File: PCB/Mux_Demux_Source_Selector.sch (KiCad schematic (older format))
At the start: 2 parts, among them U3 4052

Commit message: Libraries and footprints adjustments. New connectors (4 pins main, 2 pins debug and 6 pins isp). New source input cap.
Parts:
- R1: symbol R-RESCUE-ArduBooster -> R
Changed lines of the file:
@@
 EESchema Schematic File Version 2
-LIBS:ArduBooster-rescue
 LIBS:power
 LIBS:device
@@
 Rev "1.0"
 Comp ""
-Comment1 "If OUTPUT_SELECTION is \"0\", pedal signal is used."
-Comment2 "If OUTPUT_SELECTION is \"1\", Arduino signal is used."
-Comment3 ""
-Comment4 ""
+Comment1 "If OUTPUT_SELECTION is \"0\", pedal signal is used"
+Comment2 "If OUTPUT_SELECTION is \"1\", Arduino signal is used"
+Comment3 "Used as workaround to Arduino boot dalay"
+Comment4 "Select output source"
 $EndDescr
 $Comp
@@
 Connection ~ 4950 4400
 $Comp
-L R-RESCUE-ArduBooster R1
+L R R1
 U 1 1 54D7D7B4
 P 4700 4350
@@
 	4850 4050 4200 4050
 Wire Wire Line
-	4700 4050 4700 4100
+	4700 4050 4700 4200
 Wire Wire Line
-	4700 4650 4700 4600
+	4700 4650 4700 4500
 Connection ~ 4950 4650
 Connection ~ 4700 4050

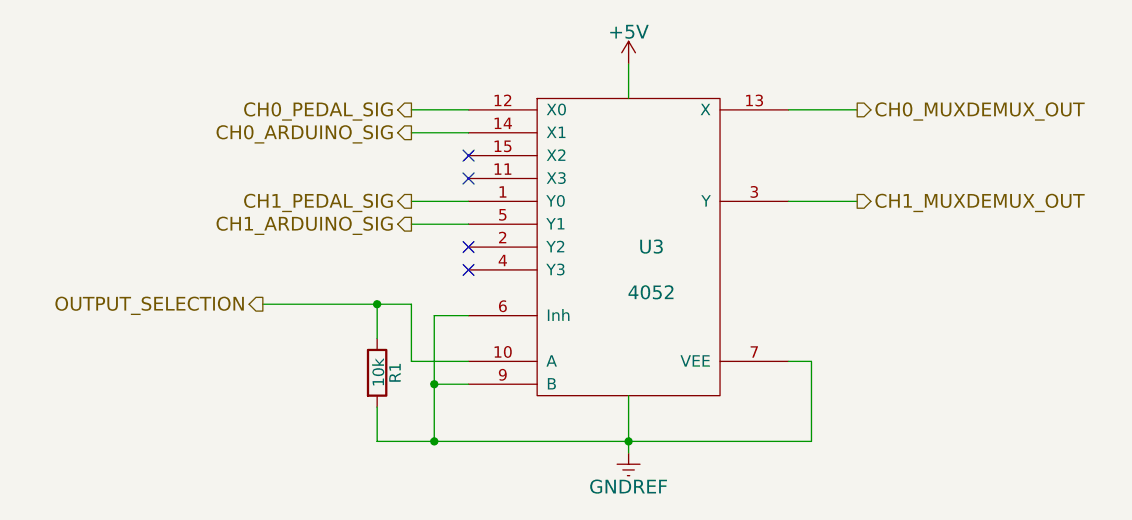
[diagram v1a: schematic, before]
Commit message: New connectors connection. Labels corrections (direction).
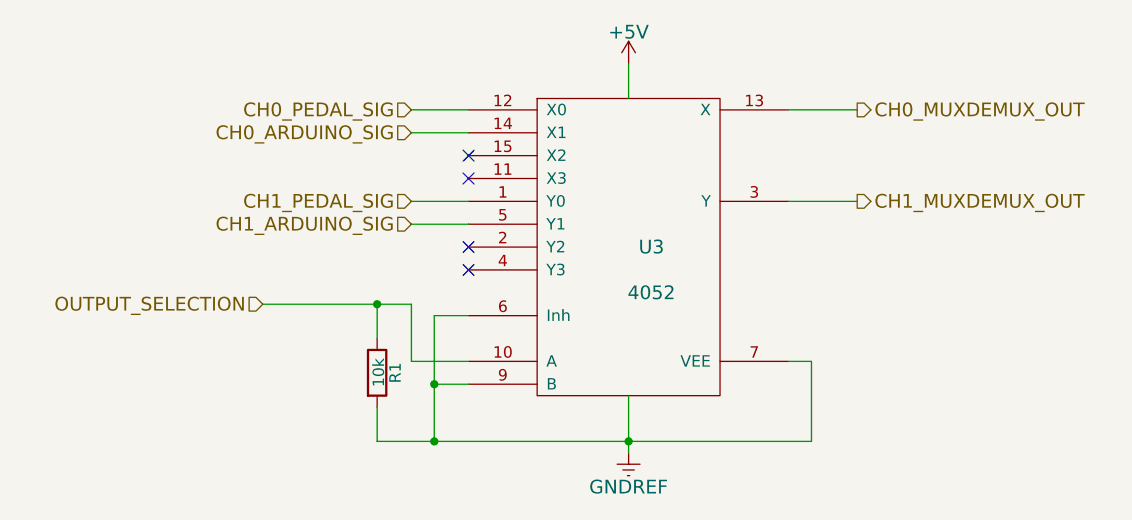
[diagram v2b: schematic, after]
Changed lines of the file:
@@
 $EndComp
 $Comp
-L GNDREF #PWR011
+L GNDREF #PWR013
 U 1 1 54D7D759
 P 5800 4700
-F 0 "#PWR011" H 5800 4450 60  0001 C CNN
+F 0 "#PWR013" H 5800 4450 60  0001 C CNN
 F 1 "GNDREF" H 5800 4550 60  0000 C CNN
 F 2 "" H 5800 4700 60  0000 C CNN
@@
 NoConn ~ 5100 3400
 $Comp
-L +5V #PWR012
+L +5V #PWR014
 U 1 1 54D7DB5C
 P 5800 3000
-F 0 "#PWR012" H 5800 2850 60  0001 C CNN
+F 0 "#PWR014" H 5800 2850 60  0001 C CNN
 F 1 "+5V" H 5800 3140 60  0000 C CNN
 F 2 "" H 5800 3000 60  0000 C CNN
@@
 Wire Wire Line
 	5800 3000 5800 3150
-Text HLabel 4850 3200 0    60   Output ~ 0
+Text HLabel 4850 3200 0    60   Input ~ 0
 CH0_PEDAL_SIG
-Text HLabel 4850 3300 0    60   Output ~ 0
+Text HLabel 4850 3300 0    60   Input ~ 0
 CH0_ARDUINO_SIG
-Text HLabel 4850 3600 0    60   Output ~ 0
+Text HLabel 4850 3600 0    60   Input ~ 0
 CH1_PEDAL_SIG
-Text HLabel 4850 3700 0    60   Output ~ 0
+Text HLabel 4850 3700 0    60   Input ~ 0
 CH1_ARDUINO_SIG
-Text HLabel 4200 4050 0    60   Output ~ 0
+Text HLabel 4200 4050 0    60   Input ~ 0
 OUTPUT_SELECTION
 Text HLabel 6800 3600 2    60   Output ~ 0

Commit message: Correct DIP sockets footprints.
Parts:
- U3: footprint Sockets_DIP:DIP-16__300 -> Housings_DIP:DIP-16_W7.62mm_LongPads
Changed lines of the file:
@@
 F 0 "U3" H 5900 3800 60  0000 C CNN
 F 1 "4052" H 5900 3600 60  0000 C CNN
-F 2 "Sockets_DIP:DIP-16__300" H 5800 3800 60  0001 C CNN
+F 2 "Housings_DIP:DIP-16_W7.62mm_LongPads" H 5800 3800 60  0001 C CNN
 F 3 "" H 5800 3800 60  0000 C CNN
 	1    5800 3800

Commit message: Last commit before Mux/Demux removel. Single layer PCB incompete (3 wires). Add ADC input filter.
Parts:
- R1: footprint Discret:R3 -> Resistors_THT:R_Axial_DIN0207_L6.3mm_D2.5mm_P2.54mm_Vertical
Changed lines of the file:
@@
 F 0 "R1" V 4780 4350 50  0000 C CNN
 F 1 "10k" V 4707 4351 50  0000 C CNN
-F 2 "Discret:R3" V 4630 4350 30  0001 C CNN
+F 2 "Resistors_THT:R_Axial_DIN0207_L6.3mm_D2.5mm_P2.54mm_Vertical" V 4630 4350 30  0001 C CNN
 F 3 "" H 4700 4350 30  0000 C CNN
 	1    4700 4350
